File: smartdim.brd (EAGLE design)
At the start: 38.1 x 10.2 mm, 8 parts, among them Q1 N-HEXFET-2D_SOT232-, U1 Tiny85-20-SMT

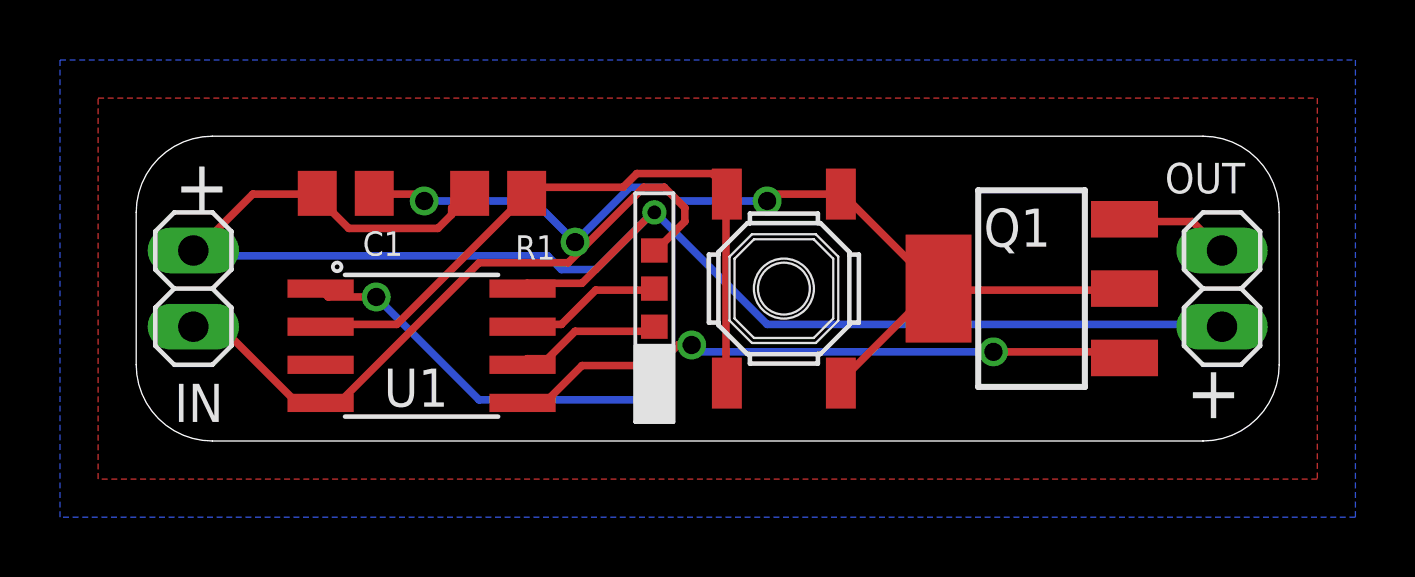
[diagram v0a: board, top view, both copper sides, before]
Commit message: Remove unnecessary pullup
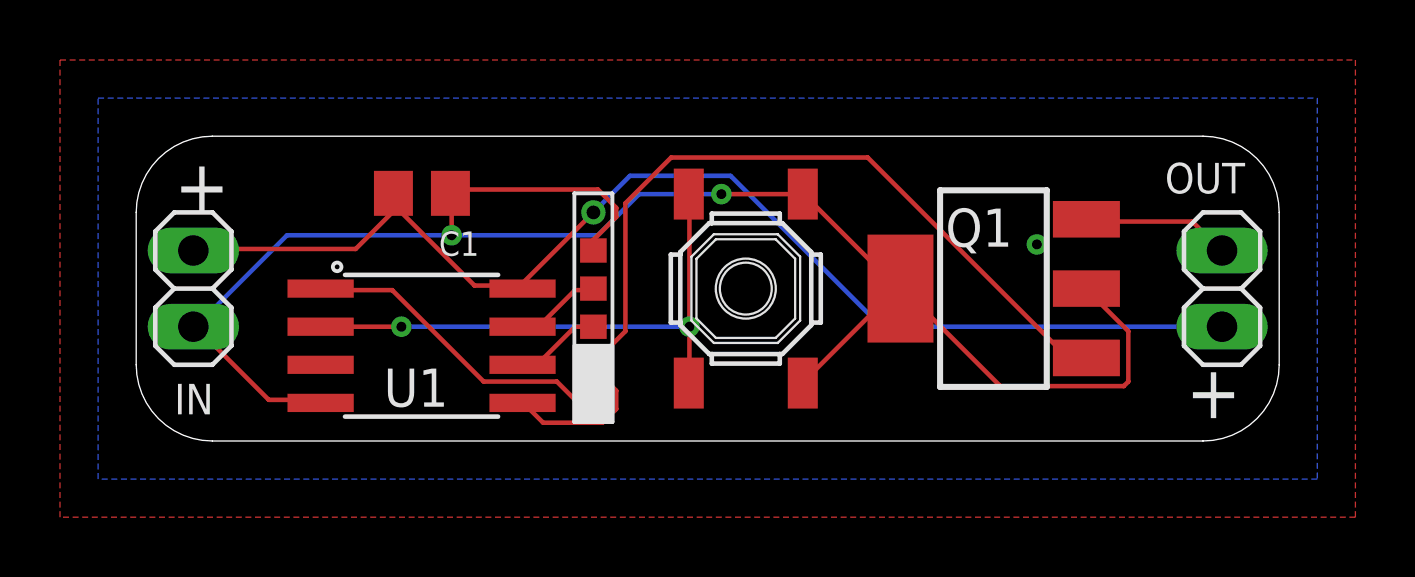
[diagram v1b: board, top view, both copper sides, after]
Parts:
- removed R1: 4K7, rcl:R0805
- moved C1 2.54 mm to (9.53, 8.26)
- moved ICSP 2.03 mm to (15.2, 5.08)
- moved Q1 1.27 mm to (28.6, 5.08)
- moved SW1 1.27 mm to (20.3, 5.08)
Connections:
- net +5V: no longer R1.2
- net USER_INPUT: no longer R1.1
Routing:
- net +5V: track 53.6 -> 40.9 mm
- net MOSI/PWM: track 21.1 -> 30.0 mm, vias 2 -> 0
- net USER_INPUT: track 22.5 -> 18.6 mm, vias 0 -> 2
- net GND: track 55.6 -> 58.5 mm, vias 3 -> 2
- net MISO: track 4.95 -> 2.88 mm
- net NRES: track 12.7 -> 10.7 mm, vias 1 -> 0
- net SCK: track 4.90 -> 2.92 mm
- net PWM_VSS: track 3.66 -> 4.97 mm
- added copper zone on layer 16, net N$1
- added copper zone on layer 1, net N$2
- removed copper zone on layer 1, net GND
- removed copper zone on layer 16, net GND
